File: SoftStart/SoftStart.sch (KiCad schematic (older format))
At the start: 38 parts, among them J1 LIVE, J10 LIVE, J11 Conn_01x02, J12 NEUTRAL, J13 NEUTRAL, J14 NEUTRAL, J15 NEUTRAL, J16 NEUTRAL, J17 NEUTRAL, J2 NEUTRAL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

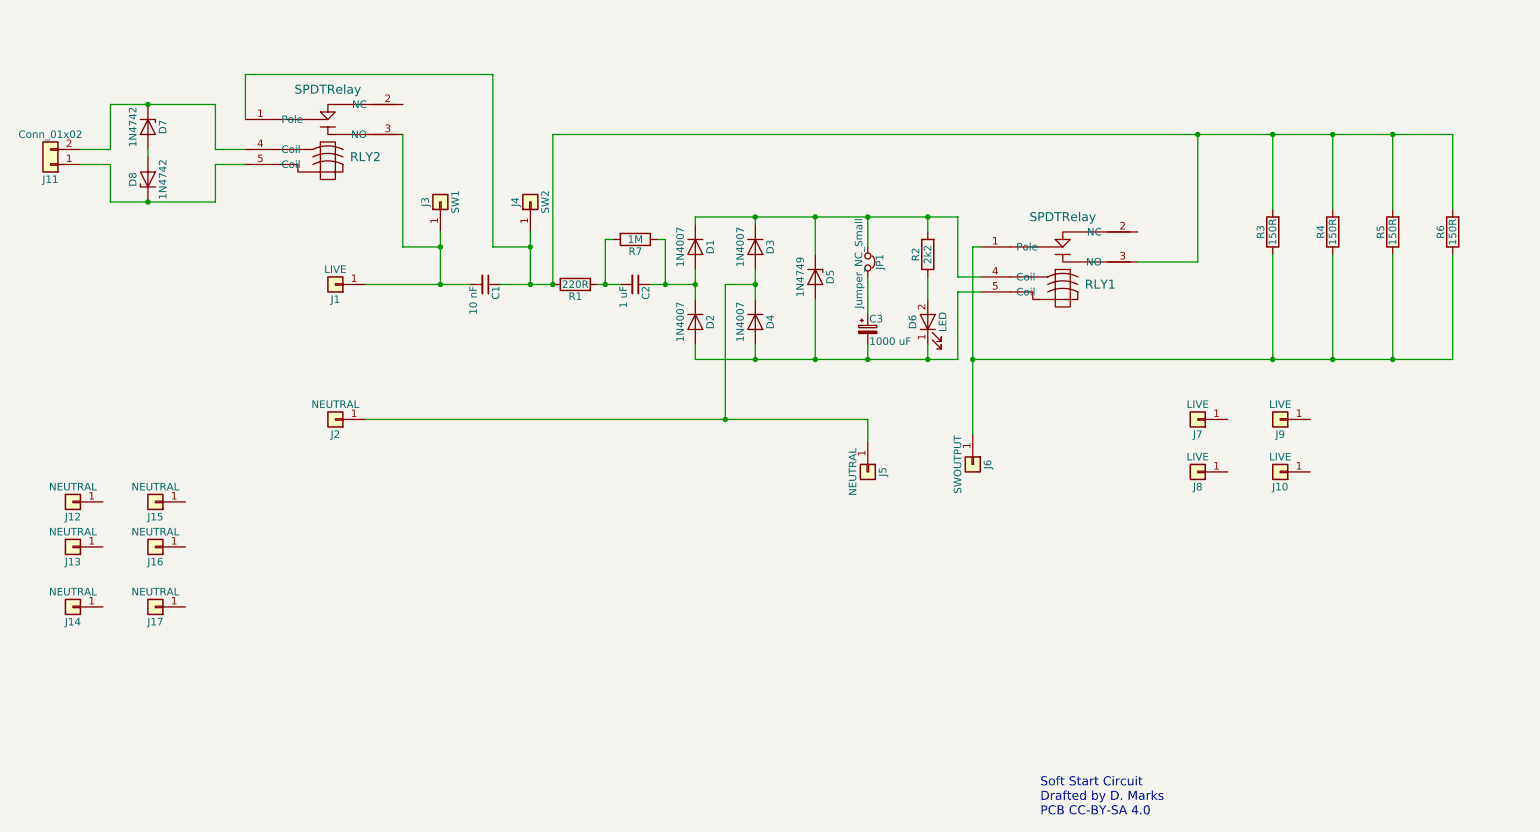
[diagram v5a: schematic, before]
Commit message: Modified soft start to have wire jumper over resistors
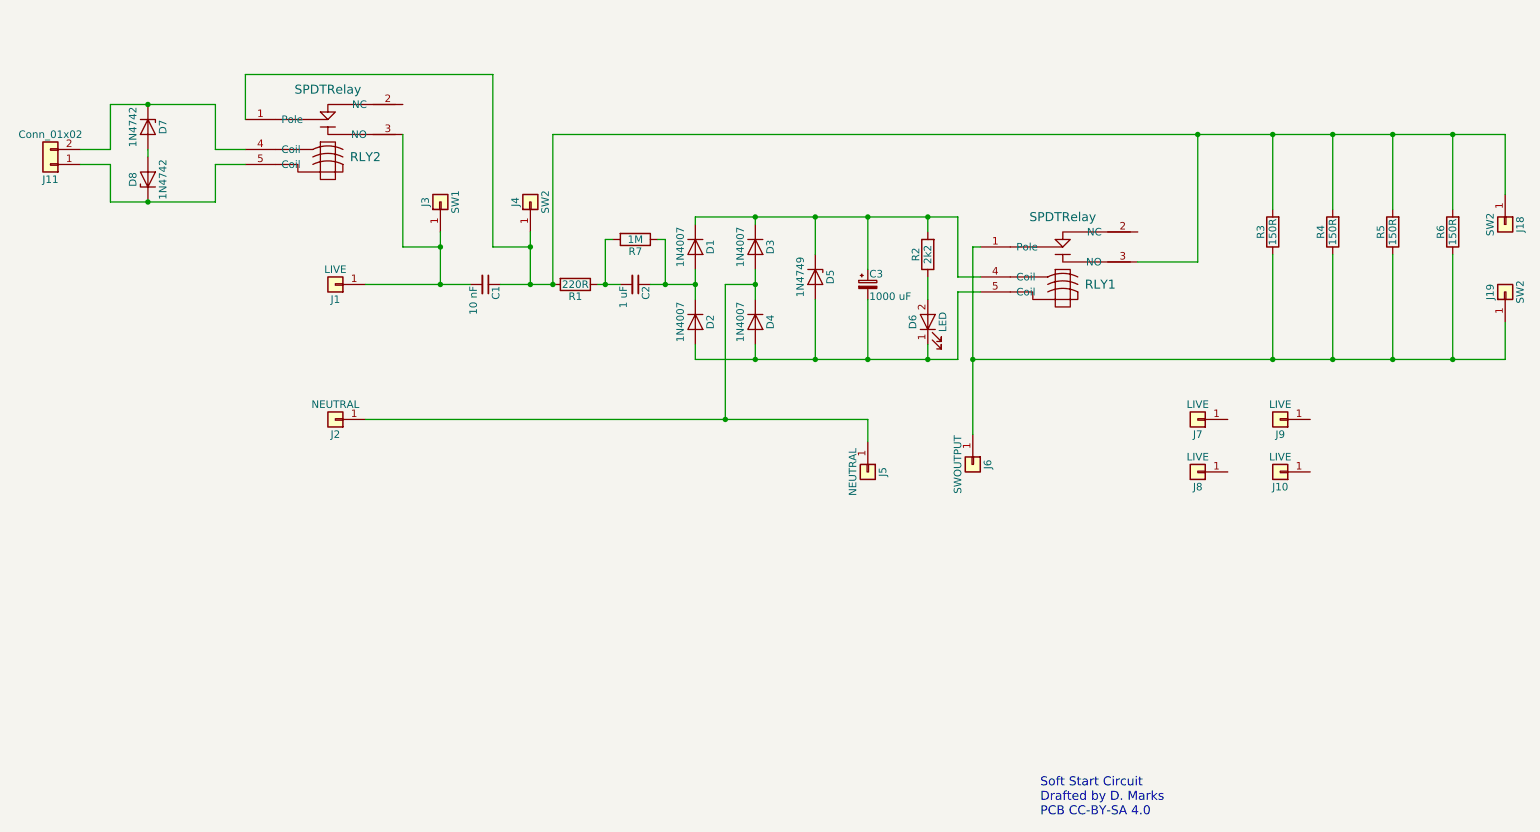
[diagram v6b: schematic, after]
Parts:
- removed J12, J13, J14, J15, J16, J17: NEUTRAL, Connectors:1pin, symbol Conn_01x01
- removed JP1: Jumper_NC_Small, Pin_Headers:Pin_Header_Straight_1x02_Pitch2.54mm, symbol Jumper_NC_Small
- added J18, J19: SW2, Connectors:1pin, symbol Conn_01x01
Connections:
- net at J6.1 (Pin_1), R3.1, R4.1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: now also J19.1 (Pin_1)
- net at C1.1, J4.1 (Pin_1), R1.2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: now also J18.1 (Pin_1)
- net at D1.1 (K), D3.1 (K), D5.1 (K)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: now also C3.1
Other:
- moved on the sheet: C3
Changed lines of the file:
@@
 L CP_Small C3
 U 1 1 5F4113E8
-P 6650 3700
-F 0 "C3" H 6660 3770 50  0000 L CNN
-F 1 "1000 uF" H 6660 3620 50  0000 L CNN
-F 2 "Capacitors_THT:CP_Radial_D10.0mm_P5.00mm" H 6650 3700 50  0001 C CNN
-F 3 "" H 6650 3700 50  0001 C CNN
-F 4 "C338226" H 6650 3700 60  0001 C CNN "LCSC"
-	1    6650 3700
+P 6650 3400
+F 0 "C3" H 6660 3470 50  0000 L CNN
+F 1 "1000 uF" H 6660 3320 50  0000 L CNN
+F 2 "Capacitors_THT:CP_Radial_D10.0mm_P5.00mm" H 6650 3400 50  0001 C CNN
+F 3 "" H 6650 3400 50  0001 C CNN
+F 4 "C338226" H 6650 3400 60  0001 C CNN "LCSC"
+	1    6650 3400
 	1    0    0    -1
 $EndComp
@@
 	0    1    1    0
 $EndComp
-$Comp
-L Conn_01x01 J12
-U 1 1 5F6D1F0A
-P 1350 4850
-F 0 "J12" H 1350 4950 50  0000 C CNN
-F 1 "NEUTRAL" H 1350 4750 50  0000 C CNN
-F 2 "Connectors:1pin" H 1350 4850 50  0001 C CNN
-F 3 "" H 1350 4850 50  0001 C CNN
-	1    1350 4850
-	-1   0    0    1
-$EndComp
-$Comp
-L Conn_01x01 J13
-U 1 1 5F6D1F9C
-P 1350 5150
-F 0 "J13" H 1350 5250 50  0000 C CNN
-F 1 "NEUTRAL" H 1350 5050 50  0000 C CNN
-F 2 "Connectors:1pin" H 1350 5150 50  0001 C CNN
-F 3 "" H 1350 5150 50  0001 C CNN
-	1    1350 5150
-	-1   0    0    1
-$EndComp
-$Comp
-L Conn_01x01 J15
-U 1 1 5F6D2021
-P 1900 4850
-F 0 "J15" H 1900 4950 50  0000 C CNN
-F 1 "NEUTRAL" H 1900 4750 50  0000 C CNN
-F 2 "Connectors:1pin" H 1900 4850 50  0001 C CNN
-F 3 "" H 1900 4850 50  0001 C CNN
-	1    1900 4850
-	-1   0    0    1
-$EndComp
-$Comp
-L Conn_01x01 J16
-U 1 1 5F6D20A5
-P 1900 5150
-F 0 "J16" H 1900 5250 50  0000 C CNN
-F 1 "NEUTRAL" H 1900 5050 50  0000 C CNN
-F 2 "Connectors:1pin" H 1900 5150 50  0001 C CNN
-F 3 "" H 1900 5150 50  0001 C CNN
-	1    1900 5150
-	-1   0    0    1
-$EndComp
-$Comp
-L Conn_01x01 J14
-U 1 1 5F6D214B
-P 1350 5550
-F 0 "J14" H 1350 5650 50  0000 C CNN
-F 1 "NEUTRAL" H 1350 5450 50  0000 C CNN
-F 2 "Connectors:1pin" H 1350 5550 50  0001 C CNN
-F 3 "" H 1350 5550 50  0001 C CNN
-	1    1350 5550
-	-1   0    0    1
-$EndComp
-$Comp
-L Conn_01x01 J17
-U 1 1 5F6D21D3
-P 1900 5550
-F 0 "J17" H 1900 5650 50  0000 C CNN
-F 1 "NEUTRAL" H 1900 5450 50  0000 C CNN
-F 2 "Connectors:1pin" H 1900 5550 50  0001 C CNN
-F 3 "" H 1900 5550 50  0001 C CNN
-	1    1900 5550
-	-1   0    0    1
-$EndComp
-$Comp
-L Jumper_NC_Small JP1
-U 1 1 5F979283
-P 6650 3250
-F 0 "JP1" H 6650 3330 50  0000 C CNN
-F 1 "Jumper_NC_Small" H 6660 3190 50  0000 C CNN
-F 2 "Pin_Headers:Pin_Header_Straight_1x02_Pitch2.54mm" H 6650 3250 50  0001 C CNN
-F 3 "" H 6650 3250 50  0001 C CNN
-	1    6650 3250
-	0    1    1    0
-$EndComp
 Wire Wire Line
 	3800 3050 3800 3400
@@
 Connection ~ 6300 2950
 Wire Wire Line
-	6650 3900 6650 3800
+	6650 3900 6650 3500
 Connection ~ 6300 3900
 Connection ~ 6650 2950
@@
 Connection ~ 7050 3900
 Wire Wire Line
-	4550 2400 10550 2400
+	4550 2400 10900 2400
 Wire Wire Line
 	8850 2400 8850 3250
@@
 	9350 2400 9350 2900
 Wire Wire Line
-	7350 3900 10550 3900
+	7350 3900 10900 3900
 Wire Wire Line
 	9350 3900 9350 3200
@@
 Connection ~ 1850 2850
 Wire Wire Line
-	6650 3150 6650 2950
-Wire Wire Line
-	6650 3350 6650 3600
+	6650 2950 6650 3300
+$Comp
+L Conn_01x01 J19
+U 1 1 5FF159C1
+P 10900 3450
+F 0 "J19" H 10900 3550 50  0000 C CNN
+F 1 "SW2" H 10900 3350 50  0000 C CNN
+F 2 "Connectors:1pin" H 10900 3450 50  0001 C CNN
+F 3 "" H 10900 3450 50  0001 C CNN
+	1    10900 3450
+	0    -1   -1   0
+$EndComp
+Wire Wire Line
+	10900 3900 10900 3650
+Connection ~ 10550 3900
+$Comp
+L Conn_01x01 J18
+U 1 1 5FF15C8B
+P 10900 3000
+F 0 "J18" H 10900 3100 50  0000 C CNN
+F 1 "SW2" H 10900 2900 50  0000 C CNN
+F 2 "Connectors:1pin" H 10900 3000 50  0001 C CNN
+F 3 "" H 10900 3000 50  0001 C CNN
+	1    10900 3000
+	0    1    1    0
+$EndComp
+Wire Wire Line
+	10900 2400 10900 2800
+Connection ~ 10550 2400
 $EndSCHEMATC

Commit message: Additions of optional zener diodes to limit current surges
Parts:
- J1, J18, J19, J2, J3, J4, J5, J6: footprint Connectors:1pin -> SoftStart:SpadeTerminal635
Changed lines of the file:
@@
 F 0 "J1" H 3100 3500 50  0000 C CNN
 F 1 "LIVE" H 3100 3300 50  0000 C CNN
-F 2 "Connectors:1pin" H 3100 3400 50  0001 C CNN
+F 2 "SoftStart:SpadeTerminal635" H 3100 3400 50  0001 C CNN
 F 3 "" H 3100 3400 50  0001 C CNN
 	1    3100 3400
@@
 F 0 "J2" H 3100 4400 50  0000 C CNN
 F 1 "NEUTRAL" H 3100 4200 50  0000 C CNN
-F 2 "Connectors:1pin" H 3100 4300 50  0001 C CNN
+F 2 "SoftStart:SpadeTerminal635" H 3100 4300 50  0001 C CNN
 F 3 "" H 3100 4300 50  0001 C CNN
 	1    3100 4300
@@
 F 0 "J3" H 3800 2950 50  0000 C CNN
 F 1 "SW1" H 3800 2750 50  0000 C CNN
-F 2 "Connectors:1pin" H 3800 2850 50  0001 C CNN
+F 2 "SoftStart:SpadeTerminal635" H 3800 2850 50  0001 C CNN
 F 3 "" H 3800 2850 50  0001 C CNN
 	1    3800 2850
@@
 F 0 "J4" H 4400 2950 50  0000 C CNN
 F 1 "SW2" H 4400 2750 50  0000 C CNN
-F 2 "Connectors:1pin" H 4400 2850 50  0001 C CNN
+F 2 "SoftStart:SpadeTerminal635" H 4400 2850 50  0001 C CNN
 F 3 "" H 4400 2850 50  0001 C CNN
 	1    4400 2850
@@
 F 0 "J6" H 7350 4700 50  0000 C CNN
 F 1 "SWOUTPUT" H 7350 4500 50  0000 C CNN
-F 2 "Connectors:1pin" H 7350 4600 50  0001 C CNN
+F 2 "SoftStart:SpadeTerminal635" H 7350 4600 50  0001 C CNN
 F 3 "" H 7350 4600 50  0001 C CNN
 	1    7350 4600
@@
 F 0 "J5" H 6650 4750 50  0000 C CNN
 F 1 "NEUTRAL" H 6650 4550 50  0000 C CNN
-F 2 "Connectors:1pin" H 6650 4650 50  0001 C CNN
+F 2 "SoftStart:SpadeTerminal635" H 6650 4650 50  0001 C CNN
 F 3 "" H 6650 4650 50  0001 C CNN
 	1    6650 4650
@@
 F 0 "J19" H 10900 3550 50  0000 C CNN
 F 1 "SW2" H 10900 3350 50  0000 C CNN
-F 2 "Connectors:1pin" H 10900 3450 50  0001 C CNN
+F 2 "SoftStart:SpadeTerminal635" H 10900 3450 50  0001 C CNN
 F 3 "" H 10900 3450 50  0001 C CNN
 	1    10900 3450
@@
 F 0 "J18" H 10900 3100 50  0000 C CNN
 F 1 "SW2" H 10900 2900 50  0000 C CNN
-F 2 "Connectors:1pin" H 10900 3000 50  0001 C CNN
+F 2 "SoftStart:SpadeTerminal635" H 10900 3000 50  0001 C CNN
 F 3 "" H 10900 3000 50  0001 C CNN
 	1    10900 3000
